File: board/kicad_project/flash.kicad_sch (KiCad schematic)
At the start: 5 parts, among them J7 Conn_01x02, U2 W25Q128JVS

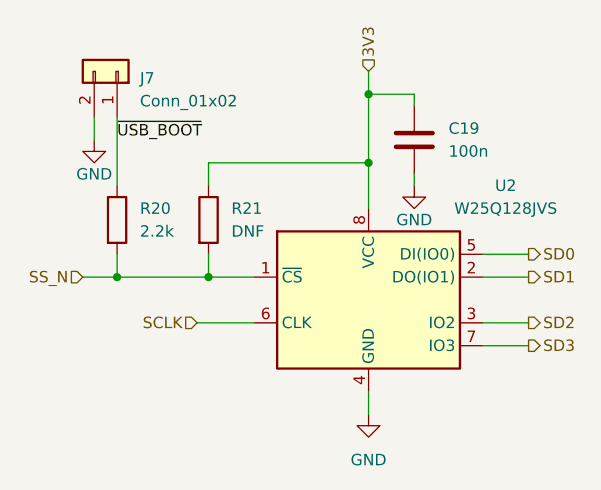
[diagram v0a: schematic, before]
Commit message: Add LCSC part numbers to board file
* Also replaced flash chip with cheaper/smaller HG25Q16 that should be
  pin compatible
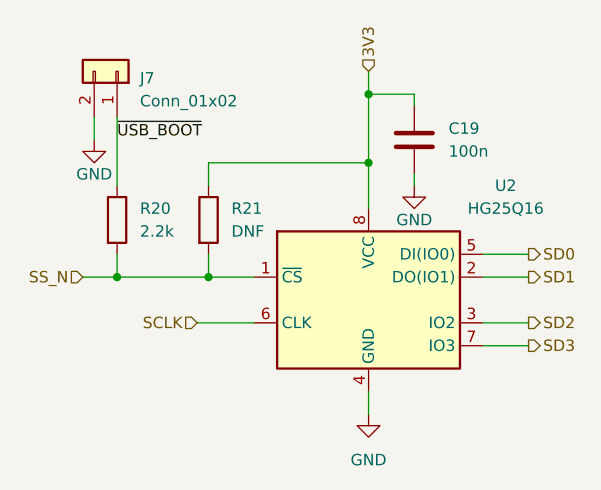
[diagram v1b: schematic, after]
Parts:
- U2: value W25Q128JVS -> HG25Q16; LCSC Part C97521 -> C2688463
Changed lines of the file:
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@@
       (effects (font (size 1.27 1.27)))
     )
-    (property "Value" "W25Q128JVS" (id 1) (at 154.94 83.82 0)
+    (property "Value" "HG25Q16" (id 1) (at 154.94 83.82 0)
       (effects (font (size 1.27 1.27)))
     )
@@
       (effects (font (size 1.27 1.27)) hide)
     )
-    (property "Datasheet" "http://www.winbond.com/resource-files/w25q128jv_dtr%20revc%2003272018%20plus.pdf" (id 3) (at 139.7 93.98 0)
+    (property "Datasheet" "https://datasheet.lcsc.com/lcsc/2103251934_HGSEMI-HG25Q16M-TR_C2688463.pdf" (id 3) (at 139.7 93.98 0)
       (effects (font (size 1.27 1.27)) hide)
     )
-    (property "LCSC Part" "C97521" (id 4) (at 139.7 93.98 0)
+    (property "LCSC Part" "C2688463" (id 4) (at 139.7 93.98 0)
       (effects (font (size 1.27 1.27)) hide)
     )
